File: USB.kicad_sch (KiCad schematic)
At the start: 16 parts, among them J6 USB_C_Receptacle_USB2.0_16P, U13 TPD4EUSB30, U6 CP2102N-A02-GQFN24R

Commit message: fix: BOM issue
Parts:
- D5: MPN LTST-C191KFKT -> LTST-C191KFKT
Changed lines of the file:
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@@
 			)
 		)
-		(property "MPN" " LTST-C191KFKT"
+		(property "MPN" "LTST-C191KFKT"
 			(at 226.06 137.16 0)
 			(effects

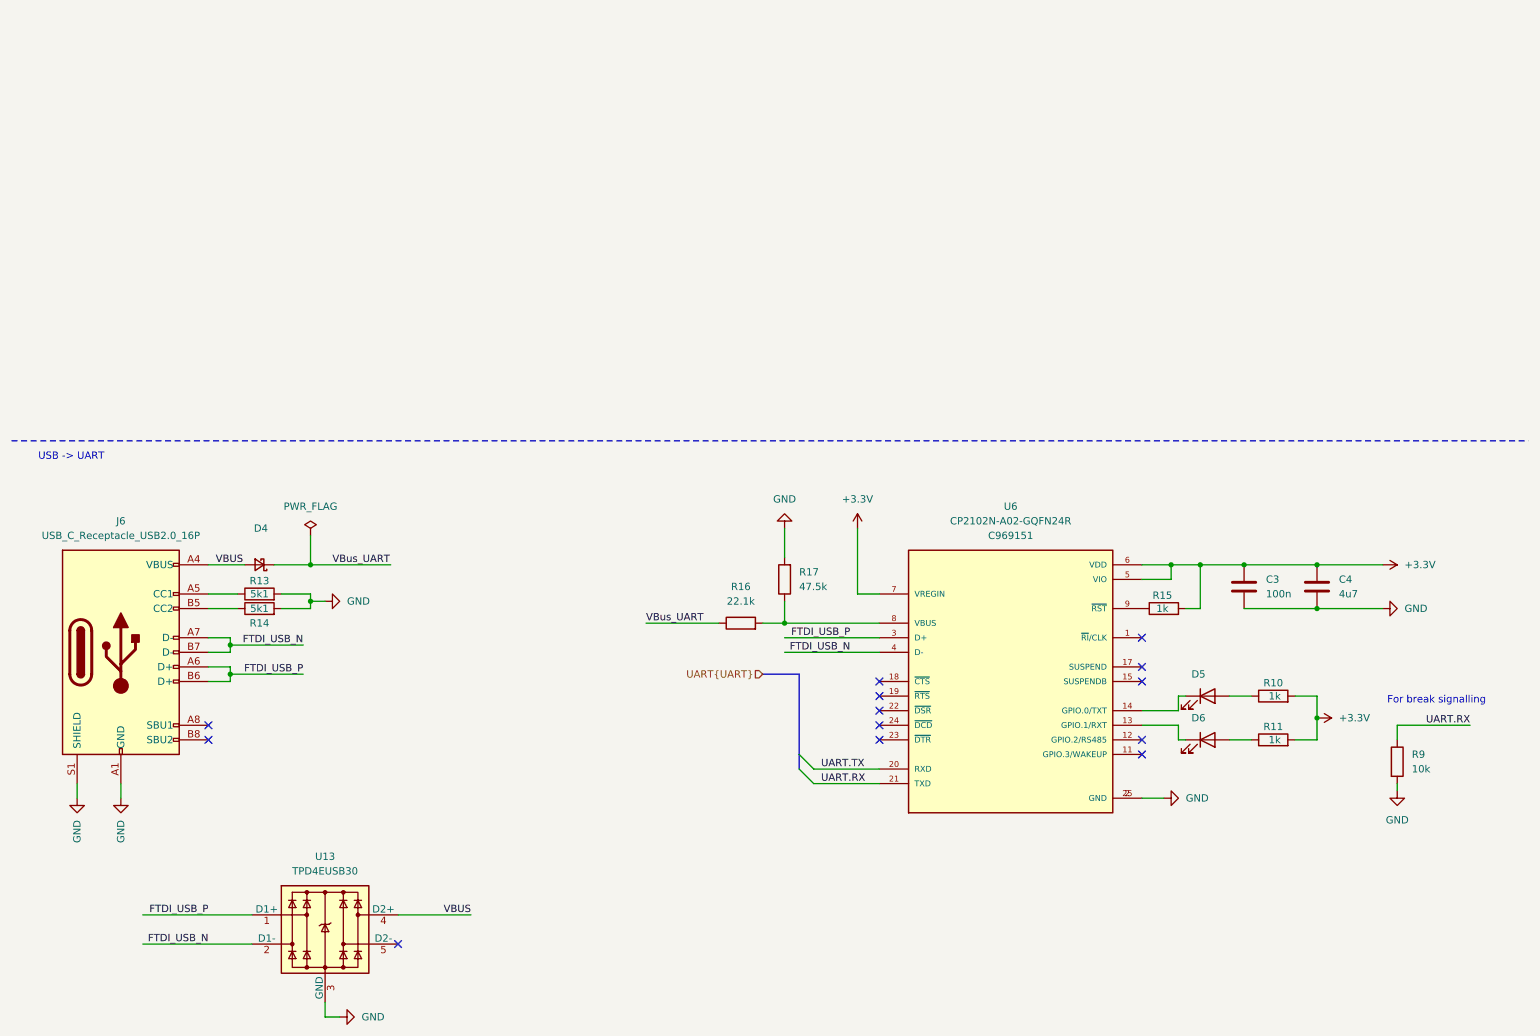
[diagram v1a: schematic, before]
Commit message: feat: use hardware components
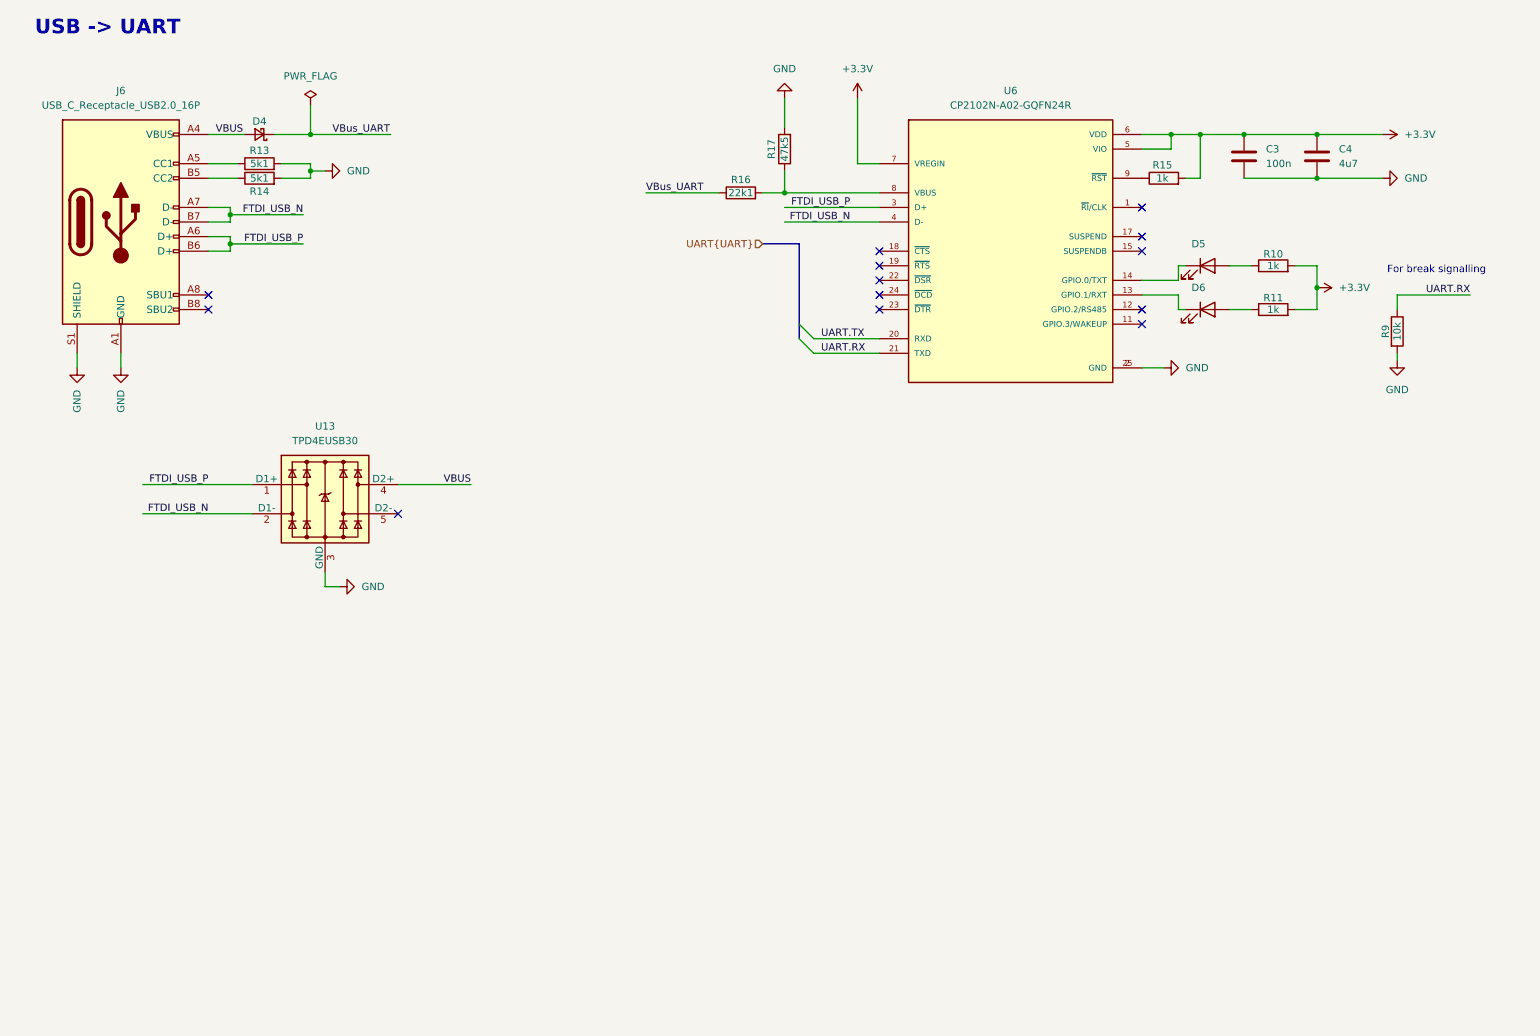
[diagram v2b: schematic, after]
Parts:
- C3: footprint HomeLabIO:C_0402_1005Metric -> Hardware Components:C_0402_1005Metric; symbol HomeLabIO:C -> Hardware Components:C_100n_0402_16V
- C4: footprint HomeLabIO:C_0402_1005Metric -> Hardware Components:C_0402_1005Metric; symbol HomeLabIO:C -> Hardware Components:C_4u7_0402_16V
- D4: footprint Diode_SMD:D_0402_1005Metric -> Hardware Components:D_0402_1005Metric; symbol Device:D_Schottky_Small -> Hardware Components:D_0402_30V_100mA
- D5, D6: footprint LED_SMD:LED_0603_1608Metric -> Hardware Components:LED_0603_1608Metric; symbol HomeLabIO:LED -> Hardware Components:LED_O_0603_LTST-C191KFKT
- J6: footprint Connector_USB:USB_C_Receptacle_HRO_TYPE-C-31-M-12 -> Hardware Components:USB_C_Receptacle_HRO_TYPE-C-31-M-12; symbol Connector:USB_C_Receptacle_USB2.0_16P -> Hardware Components:USB_C_Receptacle_HRO_TYPE-C-31-M-12
- R10, R11, R15: footprint HomeLabIO:R_0402_1005Metric -> Hardware Components:R_0402_1005Metric; symbol HomeLabIO:R -> Hardware Components:R_1k_0402_75V
- R13, R14: footprint HomeLabIO:R_0402_1005Metric -> Hardware Components:R_0402_1005Metric; symbol HomeLabIO:R -> Hardware Components:R_5k1_0402_50V
- R16: value 22.1k -> 22k1; footprint HomeLabIO:R_0402_1005Metric -> Hardware Components:R_0402_1005Metric; symbol HomeLabIO:R -> Hardware Components:R_22k1_0402_50V
- R17: value 47.5k -> 47k5; footprint HomeLabIO:R_0402_1005Metric -> Hardware Components:R_0402_1005Metric; symbol HomeLabIO:R -> Hardware Components:R_47k5_0402_50V
- R9: footprint HomeLabIO:R_0402_1005Metric -> Hardware Components:R_0402_1005Metric; symbol HomeLabIO:R -> Hardware Components:R_10k_0402_50V
- U13: footprint Package_SON:USON-10_2.5x1.0mm_P0.5mm -> Hardware Components:TPD4EUSB30_USON-10; symbol HomeLabIO:TPD4EUSB30 -> Hardware Components:ESD_TPD4EUSB30
- U6: footprint HomeLabIO:QFN50P400X400X80-25N -> Hardware Components:CP2102-A02-GQ-QFN-50P; symbol HomeLabIO:CP2102N-A02-GQFN24R -> Hardware Components:CP2102-A02-GQ
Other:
- moved on the sheet: C3, C4, D4, D5, D6, J6, R10, R11, R13, R14, R15, R16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

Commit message: feat: update components and README
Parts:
- D4: JLCPCB Part # C2886014 -> C2886012; MPN CDBQR0130L-HF -> CDBQC0130L-HF
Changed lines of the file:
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@@
 			)
 		)
-		(property "Description" "35V Independent Type 350mV@10mA 100mA SOD-923F  Schottky Diodes ROHS"
+		(property "Description" "-40℃~+125℃ 100mA 10uA@10V 250mV@10mA 30V 3A SOD-923F Schottky Diodes ROHS"
 			(at 60.96 39.37 0)
 			(effects
@@
 			)
 		)
-		(property "MPN" "CDBQR0130L-HF"
+		(property "MPN" "CDBQC0130L-HF "
 			(at 60.96 39.37 0)
 			(effects
@@
 			)
 		)
-		(property "JLCPCB Part #" "C2886014"
+		(property "JLCPCB Part #" "C2886012"
 			(at 60.96 39.37 0)
 			(effects
